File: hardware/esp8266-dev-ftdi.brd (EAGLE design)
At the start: 50 x 50 mm, 58 parts, among them CON1 USBMICRO-NO_CENTER-LONG_PADS

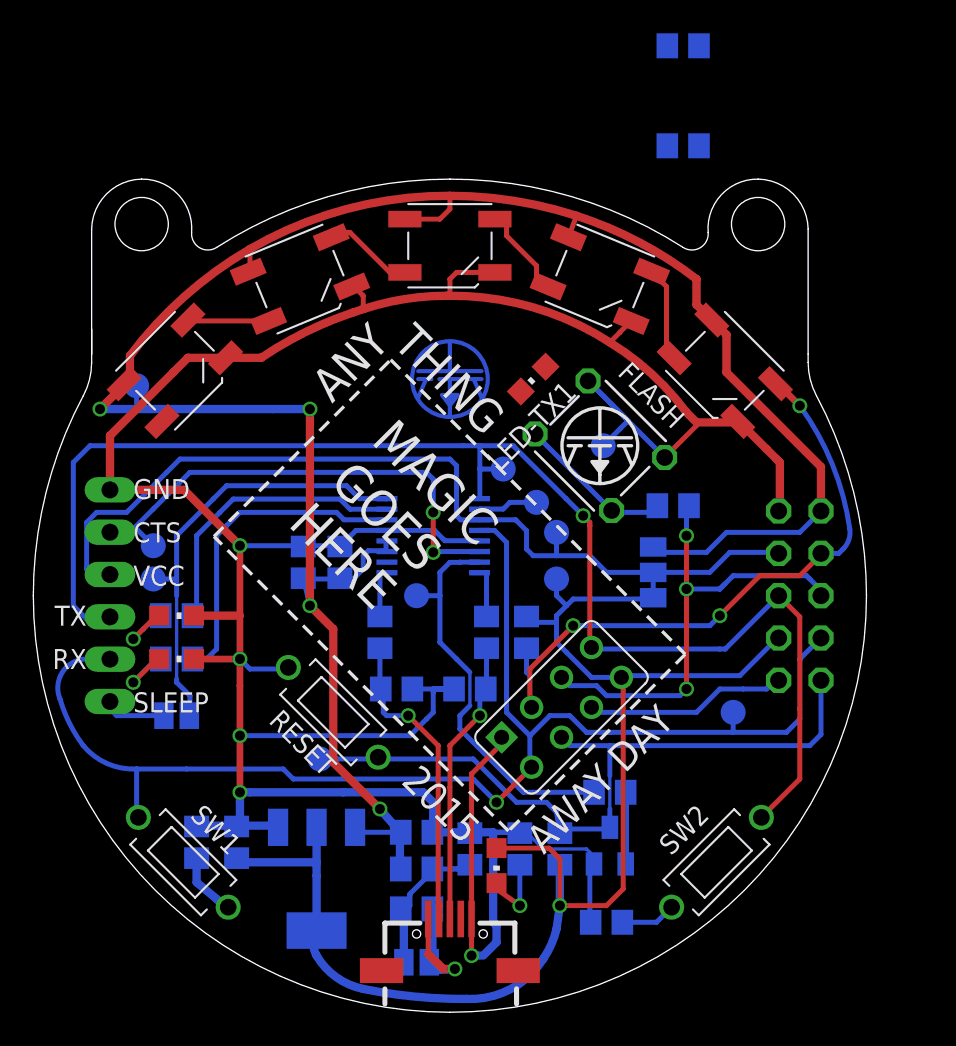
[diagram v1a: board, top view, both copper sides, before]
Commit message: basic layoutfor added components
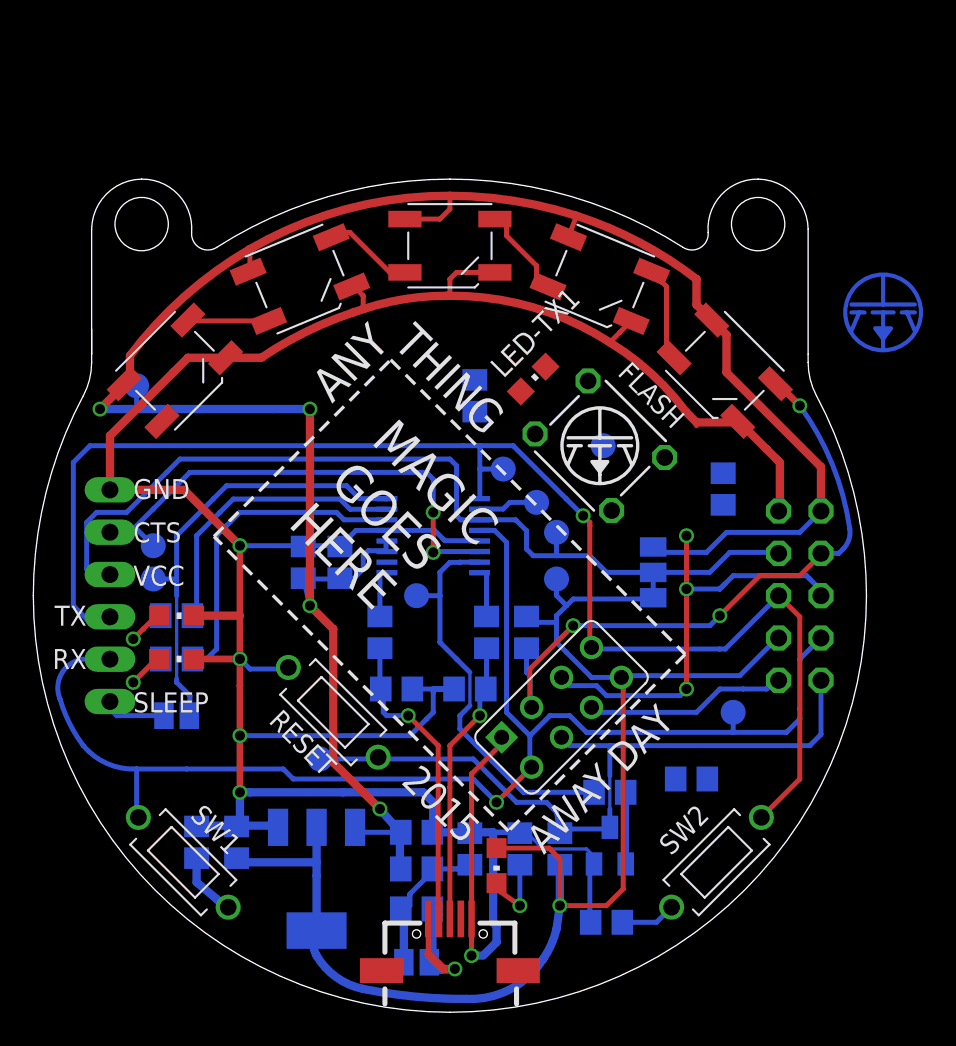
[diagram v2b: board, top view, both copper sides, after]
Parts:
- moved R12 44.0 mm to (39.5, 14.0), turned to 180 degrees
- moved U$1 26.3 mm to (51.0, 42.0)
- moved R13 19.5 mm to (26.5, 37.0), turned to 270 degrees
- moved R7 3.16 mm to (41.4, 31.4), turned to 270 degrees
- turned LED-TX1 to 315 degrees
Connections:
- net GND: now also R7.2; no longer FLASH.P$3, FLASH.P$4
- net IO0: now also FLASH.P$1, FLASH.P$2; no longer R7.1
- net N$11: now also FLASH.P$3, FLASH.P$4, R7.1; no longer FLASH.P$1, FLASH.P$2, R7.2
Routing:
- net GND: track 203.8 -> 189.2 mm
- net N$11: track 10.0 -> 0.00 mm
- net IO0: track 28.7 -> 26.8 mm
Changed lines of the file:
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@@
 <layers>
 <layer number="1" name="Top" color="4" fill="1" visible="yes" active="yes"/>
-<layer number="16" name="Bottom" color="1" fill="1" visible="no" active="yes"/>
+<layer number="16" name="Bottom" color="1" fill="1" visible="yes" active="yes"/>
 <layer number="17" name="Pads" color="2" fill="1" visible="yes" active="yes"/>
 <layer number="18" name="Vias" color="2" fill="1" visible="yes" active="yes"/>
 <layer number="19" name="Unrouted" color="6" fill="1" visible="yes" active="yes"/>
 <layer number="20" name="Dimension" color="15" fill="1" visible="yes" active="yes"/>
-<layer number="21" name="tPlace" color="7" fill="1" visible="yes" active="yes"/>
+<layer number="21" name="tPlace" color="7" fill="1" visible="no" active="yes"/>
 <layer number="22" name="bPlace" color="7" fill="1" visible="no" active="yes"/>
 <layer number="23" name="tOrigins" color="15" fill="1" visible="yes" active="yes"/>
-<layer number="24" name="bOrigins" color="15" fill="1" visible="no" active="yes"/>
+<layer number="24" name="bOrigins" color="15" fill="1" visible="yes" active="yes"/>
 <layer number="25" name="tNames" color="7" fill="1" visible="no" active="yes"/>
 <layer number="26" name="bNames" color="7" fill="1" visible="no" active="yes"/>
 <layer number="27" name="tValues" color="7" fill="1" visible="no" active="yes"/>
 <layer number="28" name="bValues" color="7" fill="1" visible="no" active="yes"/>
-<layer number="29" name="tStop" color="7" fill="3" visible="yes" active="yes"/>
+<layer number="29" name="tStop" color="7" fill="3" visible="no" active="yes"/>
 <layer number="30" name="bStop" color="7" fill="6" visible="no" active="yes"/>
 <layer number="31" name="tCream" color="7" fill="4" visible="no" active="yes"/>
@@
 <layer number="38" name="bTest" color="7" fill="1" visible="no" active="yes"/>
 <layer number="39" name="tKeepout" color="4" fill="11" visible="yes" active="yes"/>
-<layer number="40" name="bKeepout" color="1" fill="11" visible="no" active="yes"/>
+<layer number="40" name="bKeepout" color="1" fill="11" visible="yes" active="yes"/>
 <layer number="41" name="tRestrict" color="4" fill="10" visible="no" active="yes"/>
 <layer number="42" name="bRestrict" color="1" fill="10" visible="no" active="yes"/>
@@
 <attribute name="VALUE" x="31.6" y="13.6" size="1.2" layer="28" font="vector" ratio="15" rot="MR270" align="center"/>
 </element>
-<element name="R7" library="p.peter-rcl" package="R0805" value="2k" x="38.4" y="30.4" smashed="yes" rot="MR0">
-<attribute name="VALUE" x="40" y="32.2" size="1.2" layer="28" font="vector" ratio="15" rot="MR0" align="center"/>
+<element name="R7" library="p.peter-rcl" package="R0805" value="2k" x="41.4" y="31.4" smashed="yes" rot="MR270">
+<attribute name="VALUE" x="39.6" y="33" size="1.2" layer="28" font="vector" ratio="15" rot="MR270" align="center"/>
 </element>
 <element name="R8" library="p.peter-rcl" package="R0805" value="2k" x="34.6" y="13.2" smashed="yes" rot="MR180">
@@
 </element>
 <element name="U$3" library="p.peter-doc" package="LOGO-JUSTGEEK-XS" value="" x="34" y="34"/>
-<element name="U$1" library="p.peter-doc" package="LOGO-JUSTGEEK-XS-PAD" value="" x="25" y="38" rot="MR0"/>
+<element name="U$1" library="p.peter-doc" package="LOGO-JUSTGEEK-XS-PAD" value="" x="51" y="42" rot="MR0"/>
 <element name="RTS" library="testpad" package="TP15R" value="TPSQTP15R" x="30.2" y="30.6" smashed="yes" rot="MR0">
 <attribute name="TP_SIGNAL_NAME" value="" x="30.2" y="28.06" size="1" layer="38" rot="MR0"/>
@@
 <attribute name="TP_SIGNAL_NAME" value="" x="34.2" y="31.46" size="1" layer="38" rot="MR0"/>
 </element>
-<element name="R12" library="p.peter-rcl" package="R0805" value="10k" x="39" y="58" rot="MR0"/>
-<element name="R13" library="p.peter-rcl" package="R0805" value="10k" x="39" y="52" rot="MR0"/>
-<element name="LED-TX1" library="p.peter-leds" package="CHIPLED_0805" value="" x="30" y="38" rot="R135"/>
+<element name="R12" library="p.peter-rcl" package="R0805" value="10k" x="39.5" y="14" rot="MR180"/>
+<element name="R13" library="p.peter-rcl" package="R0805" value="10k" x="26.5" y="37" rot="MR270"/>
+<element name="LED-TX1" library="p.peter-leds" package="CHIPLED_0805" value="" x="30" y="38" rot="R315"/>
 </elements>
 <signals>
@@
 <contactref element="R5" pad="1"/>
 <contactref element="RF1" pad="GND"/>
-<contactref element="FLASH" pad="P$3"/>
-<contactref element="FLASH" pad="P$4"/>
 <contactref element="U$2" pad="1"/>
 <contactref element="Q1" pad="P$2"/>
@@
 <wire x1="44.8" y1="33" x2="44.8" y2="30.15" width="0.5" layer="1"/>
 <wire x1="44.8" y1="30.15" x2="44.73" y2="30.08" width="0.3" layer="1"/>
-<wire x1="37.889084375" y1="33.292890625" x2="35.6909875" y2="35.4909875" width="0.3" layer="16"/>
-<wire x1="35.6909875" y1="35.4909875" x2="33.292890625" y2="37.889084375" width="0.3" layer="16"/>
-<wire x1="33.292890625" y1="37.889084375" x2="33.310915625" y2="37.889084375" width="0.3" layer="16"/>
-<wire x1="33.310915625" y1="37.889084375" x2="35.6" y2="35.6" width="0.3" layer="16"/>
 <wire x1="39.2" y1="36" x2="39.8" y2="35.4" width="0.5" layer="1"/>
 <wire x1="39.8" y1="35.4" x2="39.8" y2="35.20380625" width="0.3" layer="1"/>
-<wire x1="39.8" y1="35.20380625" x2="37.889084375" y2="33.292890625" width="0.3" layer="1"/>
 <wire x1="11.54055625" y1="39.277815625" x2="9.277815625" y2="39.277815625" width="0.5" layer="1"/>
 <wire x1="9.277815625" y1="39.277815625" x2="8.4" y2="38.4" width="0.5" layer="1"/>
@@
 <wire x1="28.95" y1="10.6" x2="29.2" y2="10.75" width="0.2" layer="16"/>
 <contactref element="GND" pad="TP"/>
-<wire x1="34.2" y1="34" x2="35.2" y2="35" width="0.3" layer="16"/>
-<wire x1="35.2" y1="35" x2="35.6909875" y2="35.4909875" width="0.3" layer="16"/>
 <contactref element="LED-TX1" pad="C"/>
-<wire x1="15.294075" y1="20.694075" x2="15.305921875" y2="20.694075" width="0" layer="19" extent="16-16"/>
-<wire x1="29.2575375" y1="37.2575375" x2="9.8" y2="11.15" width="0" layer="19" extent="1-16"/>
+<contactref element="R7" pad="2"/>
+<wire x1="34.6" y1="40.2" x2="30.742459375" y2="38.742459375" width="0" layer="19" extent="1-1"/>
+<wire x1="15.305921875" y1="20.694075" x2="15.294075" y2="20.694075" width="0" layer="19" extent="16-16"/>
+<wire x1="41.4" y1="30.45" x2="44.73" y2="30.08" width="0" layer="19" extent="16-16"/>
+<wire x1="34.2" y1="34" x2="39.2" y2="36" width="0" layer="19" extent="1-16"/>
 </signal>
 <signal name="+5V">
@@
 <wire x1="31.4" y1="25" x2="32" y2="24.4" width="0.3" layer="16"/>
 <contactref element="R12" pad="2"/>
-<wire x1="38.05" y1="58" x2="17" y2="3.4" width="0" layer="19" extent="1-16"/>
+<wire x1="42.4" y1="20.2" x2="40.45" y2="14" width="0" layer="19" extent="16-16"/>
 </signal>
 <signal name="N$9">
@@
 <wire x1="20.6" y1="15.2" x2="17.2" y2="15.2" width="0.3" layer="16"/>
 </signal>
-<signal name="N$11">
-<contactref element="R7" pad="2"/>
-<contactref element="FLASH" pad="P$1"/>
-<contactref element="FLASH" pad="P$2"/>
-<wire x1="34.81801875" y1="30" x2="34.70710625" y2="30.1109125" width="0.3" layer="16"/>
-<wire x1="30.1109125" y1="34.70710625" x2="34.70710625" y2="30.1109125" width="0.3" layer="16"/>
-<wire x1="37.45" y1="30.4" x2="37.6" y2="30" width="0.3" layer="16"/>
-<wire x1="37.6" y1="30" x2="34.81801875" y2="30" width="0.3" layer="16"/>
-<wire x1="34.81801875" y1="30" x2="34.70710625" y2="30.1109125" width="0.3" layer="16"/>
-</signal>
 <signal name="IO2">
 <contactref element="RF1" pad="GPIO2"/>
@@
 <signal name="IO0">
 <contactref element="RF1" pad="GPIO0"/>
-<contactref element="R7" pad="1"/>
 <contactref element="JP1" pad="6"/>
 <wire x1="47.27" y1="25" x2="47.27" y2="25.33" width="0.3" layer="16"/>
@@
 <wire x1="39.2" y1="25.4" x2="39.2" y2="28.6" width="0.3" layer="1"/>
 <via x="39.2" y="28.6" extent="1-16" drill="0.6"/>
-<wire x1="39.2" y1="28.6" x2="39.2" y2="29.85" width="0.3" layer="16"/>
-<wire x1="39.2" y1="29.85" x2="39.35" y2="30.4" width="0.3" layer="16"/>
 <contactref element="R12" pad="1"/>
 <contactref element="R13" pad="2"/>
-<wire x1="39.95" y1="58" x2="31.7" y2="20.09605" width="0" layer="19" extent="1-1"/>
-<wire x1="38.05" y1="52" x2="39.95" y2="58" width="0" layer="19" extent="1-1"/>
+<contactref element="FLASH" pad="P$2"/>
+<contactref element="FLASH" pad="P$1"/>
+<wire x1="30.1109125" y1="34.70710625" x2="26.5" y2="36.05" width="0" layer="19" extent="16-16"/>
+<wire x1="34.70710625" y1="30.1109125" x2="30.1109125" y2="34.70710625" width="0" layer="19" extent="1-1"/>
+<wire x1="39.2" y1="28.6" x2="34.70710625" y2="30.1109125" width="0" layer="19" extent="1-1"/>
+<wire x1="38.55" y1="14" x2="38.8" y2="19" width="0" layer="19" extent="16-16"/>
 </signal>
 <signal name="N$1">
@@
 <contactref element="R13" pad="1"/>
 <contactref element="LED-TX1" pad="A"/>
-<wire x1="39.95" y1="52" x2="30.742459375" y2="38.742459375" width="0" layer="19" extent="1-1"/>
+<wire x1="26.5" y1="37.95" x2="29.2575375" y2="37.2575375" width="0" layer="19" extent="1-16"/>
+</signal>
+<signal name="N$11">
+<contactref element="R7" pad="1"/>
+<contactref element="FLASH" pad="P$4"/>
+<contactref element="FLASH" pad="P$3"/>
+<wire x1="37.889084375" y1="33.292890625" x2="41.4" y2="32.35" width="0" layer="19" extent="16-16"/>
+<wire x1="33.292890625" y1="37.889084375" x2="37.889084375" y2="33.292890625" width="0" layer="19" extent="1-1"/>
 </signal>
 </signals>

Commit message: added todo
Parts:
- moved U$1 26.0 mm to (25.0, 40.5)
- moved R13 1.80 mm to (25.0, 36.0), turned to 180 degrees
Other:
- board text added: "add notches for rubber bands"
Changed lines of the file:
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@@
 <layer number="20" name="Dimension" color="15" fill="1" visible="yes" active="yes"/>
 <layer number="21" name="tPlace" color="7" fill="1" visible="no" active="yes"/>
-<layer number="22" name="bPlace" color="7" fill="1" visible="no" active="yes"/>
-<layer number="23" name="tOrigins" color="15" fill="1" visible="yes" active="yes"/>
+<layer number="22" name="bPlace" color="7" fill="1" visible="yes" active="yes"/>
+<layer number="23" name="tOrigins" color="15" fill="1" visible="no" active="yes"/>
 <layer number="24" name="bOrigins" color="15" fill="1" visible="yes" active="yes"/>
 <layer number="25" name="tNames" color="7" fill="1" visible="no" active="yes"/>
-<layer number="26" name="bNames" color="7" fill="1" visible="no" active="yes"/>
+<layer number="26" name="bNames" color="7" fill="1" visible="yes" active="yes"/>
 <layer number="27" name="tValues" color="7" fill="1" visible="no" active="yes"/>
-<layer number="28" name="bValues" color="7" fill="1" visible="no" active="yes"/>
+<layer number="28" name="bValues" color="7" fill="1" visible="yes" active="yes"/>
 <layer number="29" name="tStop" color="7" fill="3" visible="no" active="yes"/>
-<layer number="30" name="bStop" color="7" fill="6" visible="no" active="yes"/>
+<layer number="30" name="bStop" color="7" fill="6" visible="yes" active="yes"/>
 <layer number="31" name="tCream" color="7" fill="4" visible="no" active="yes"/>
 <layer number="32" name="bCream" color="7" fill="5" visible="no" active="yes"/>
@@
 <layer number="37" name="tTest" color="7" fill="1" visible="no" active="yes"/>
 <layer number="38" name="bTest" color="7" fill="1" visible="no" active="yes"/>
-<layer number="39" name="tKeepout" color="4" fill="11" visible="yes" active="yes"/>
-<layer number="40" name="bKeepout" color="1" fill="11" visible="yes" active="yes"/>
+<layer number="39" name="tKeepout" color="4" fill="11" visible="no" active="yes"/>
+<layer number="40" name="bKeepout" color="1" fill="11" visible="no" active="yes"/>
 <layer number="41" name="tRestrict" color="4" fill="10" visible="no" active="yes"/>
 <layer number="42" name="bRestrict" color="1" fill="10" visible="no" active="yes"/>
 <layer number="43" name="vRestrict" color="2" fill="10" visible="no" active="yes"/>
 <layer number="44" name="Drills" color="7" fill="1" visible="no" active="yes"/>
-<layer number="45" name="Holes" color="7" fill="1" visible="yes" active="yes"/>
+<layer number="45" name="Holes" color="7" fill="1" visible="no" active="yes"/>
 <layer number="46" name="Milling" color="3" fill="1" visible="no" active="yes"/>
-<layer number="47" name="Measures" color="7" fill="1" visible="yes" active="yes"/>
+<layer number="47" name="Measures" color="7" fill="1" visible="no" active="yes"/>
 <layer number="48" name="Document" color="7" fill="1" visible="no" active="yes"/>
 <layer number="49" name="Reference" color="7" fill="1" visible="no" active="yes"/>
@@
 <wire x1="0" y1="25" x2="25" y2="0" width="0" layer="20" curve="90"/>
 <wire x1="25" y1="0" x2="50" y2="25" width="0" layer="20" curve="90"/>
+<text x="4.5" y="52" size="1.778" layer="1">add notches for rubber bands</text>
 </plain>
 <attributes>
@@
 </element>
 <element name="U$3" library="p.peter-doc" package="LOGO-JUSTGEEK-XS" value="" x="34" y="34"/>
-<element name="U$1" library="p.peter-doc" package="LOGO-JUSTGEEK-XS-PAD" value="" x="51" y="42" rot="MR0"/>
+<element name="U$1" library="p.peter-doc" package="LOGO-JUSTGEEK-XS-PAD" value="" x="25" y="40.5" rot="MR0"/>
 <element name="RTS" library="testpad" package="TP15R" value="TPSQTP15R" x="30.2" y="30.6" smashed="yes" rot="MR0">
 <attribute name="TP_SIGNAL_NAME" value="" x="30.2" y="28.06" size="1" layer="38" rot="MR0"/>
@@
 </element>
 <element name="R12" library="p.peter-rcl" package="R0805" value="10k" x="39.5" y="14" rot="MR180"/>
-<element name="R13" library="p.peter-rcl" package="R0805" value="10k" x="26.5" y="37" rot="MR270"/>
+<element name="R13" library="p.peter-rcl" package="R0805" value="10k" x="25" y="36" rot="MR180"/>
 <element name="LED-TX1" library="p.peter-leds" package="CHIPLED_0805" value="" x="30" y="38" rot="R315"/>
 </elements>
@@
 <contactref element="FLASH" pad="P$2"/>
 <contactref element="FLASH" pad="P$1"/>
-<wire x1="30.1109125" y1="34.70710625" x2="26.5" y2="36.05" width="0" layer="19" extent="16-16"/>
+<wire x1="30.1109125" y1="34.70710625" x2="25.95" y2="36" width="0" layer="19" extent="16-16"/>
 <wire x1="34.70710625" y1="30.1109125" x2="30.1109125" y2="34.70710625" width="0" layer="19" extent="1-1"/>
 <wire x1="39.2" y1="28.6" x2="34.70710625" y2="30.1109125" width="0" layer="19" extent="1-1"/>
@@
 <contactref element="R13" pad="1"/>
 <contactref element="LED-TX1" pad="A"/>
-<wire x1="26.5" y1="37.95" x2="29.2575375" y2="37.2575375" width="0" layer="19" extent="1-16"/>
+<wire x1="24.05" y1="36" x2="29.2575375" y2="37.2575375" width="0" layer="19" extent="1-16"/>
 </signal>
 <signal name="N$11">

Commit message: cleaned up schematic
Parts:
- R13: value 10k -> 470
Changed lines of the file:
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@@
 </element>
 <element name="R12" library="p.peter-rcl" package="R0805" value="10k" x="39.5" y="14" rot="MR180"/>
-<element name="R13" library="p.peter-rcl" package="R0805" value="10k" x="25" y="36" rot="MR180"/>
+<element name="R13" library="p.peter-rcl" package="R0805" value="470" x="25" y="36" rot="MR180"/>
 <element name="LED-TX1" library="p.peter-leds" package="CHIPLED_0805" value="" x="30" y="38" rot="R315"/>
 </elements>
@@
 <wire x1="28.95" y1="10.6" x2="29.2" y2="10.75" width="0.2" layer="16"/>
 <contactref element="GND" pad="TP"/>
+<contactref element="R7" pad="2"/>
 <contactref element="LED-TX1" pad="C"/>
-<contactref element="R7" pad="2"/>
-<wire x1="34.6" y1="40.2" x2="30.742459375" y2="38.742459375" width="0" layer="19" extent="1-1"/>
+<wire x1="44.73" y1="30.08" x2="41.4" y2="30.45" width="0" layer="19" extent="16-16"/>
 <wire x1="15.305921875" y1="20.694075" x2="15.294075" y2="20.694075" width="0" layer="19" extent="16-16"/>
-<wire x1="41.4" y1="30.45" x2="44.73" y2="30.08" width="0" layer="19" extent="16-16"/>
+<wire x1="30.742459375" y1="38.742459375" x2="34.6" y2="40.2" width="0" layer="19" extent="1-1"/>
 <wire x1="34.2" y1="34" x2="39.2" y2="36" width="0" layer="19" extent="1-16"/>
 </signal>
@@
 <via x="39.2" y="28.6" extent="1-16" drill="0.6"/>
 <contactref element="R12" pad="1"/>
-<contactref element="R13" pad="2"/>
 <contactref element="FLASH" pad="P$2"/>
 <contactref element="FLASH" pad="P$1"/>
-<wire x1="30.1109125" y1="34.70710625" x2="25.95" y2="36" width="0" layer="19" extent="16-16"/>
+<contactref element="R13" pad="2"/>
+<wire x1="25.95" y1="36" x2="30.1109125" y2="34.70710625" width="0" layer="19" extent="16-16"/>
 <wire x1="34.70710625" y1="30.1109125" x2="30.1109125" y2="34.70710625" width="0" layer="19" extent="1-1"/>
 <wire x1="39.2" y1="28.6" x2="34.70710625" y2="30.1109125" width="0" layer="19" extent="1-1"/>
